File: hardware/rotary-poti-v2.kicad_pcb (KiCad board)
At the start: 2 copper layers, 30 x 25 mm, 22 parts, among them P1 CON-SENSOR2, P2 DEBUG, P3 BOOT, U1 XMC1XXX24, U3 DRILL, U4 DRILL, U5 DRILL, U6 DRILL

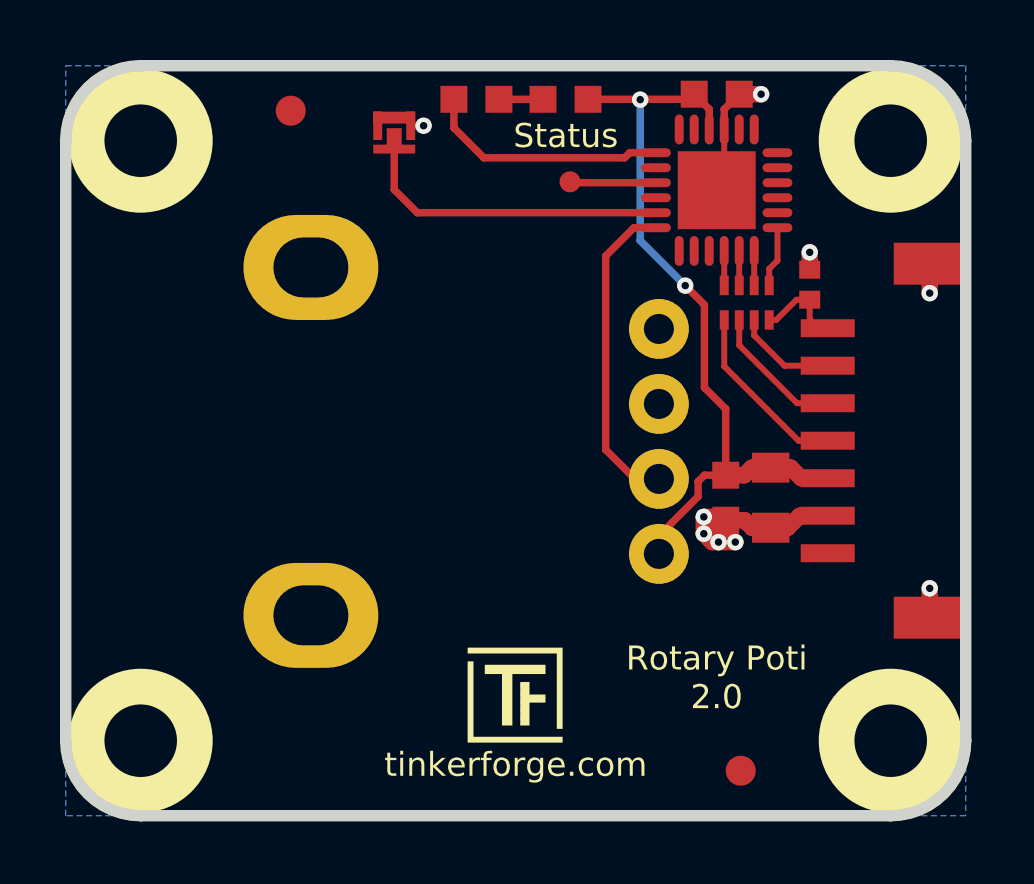
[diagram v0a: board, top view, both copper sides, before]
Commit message: Fix pin of IN_1
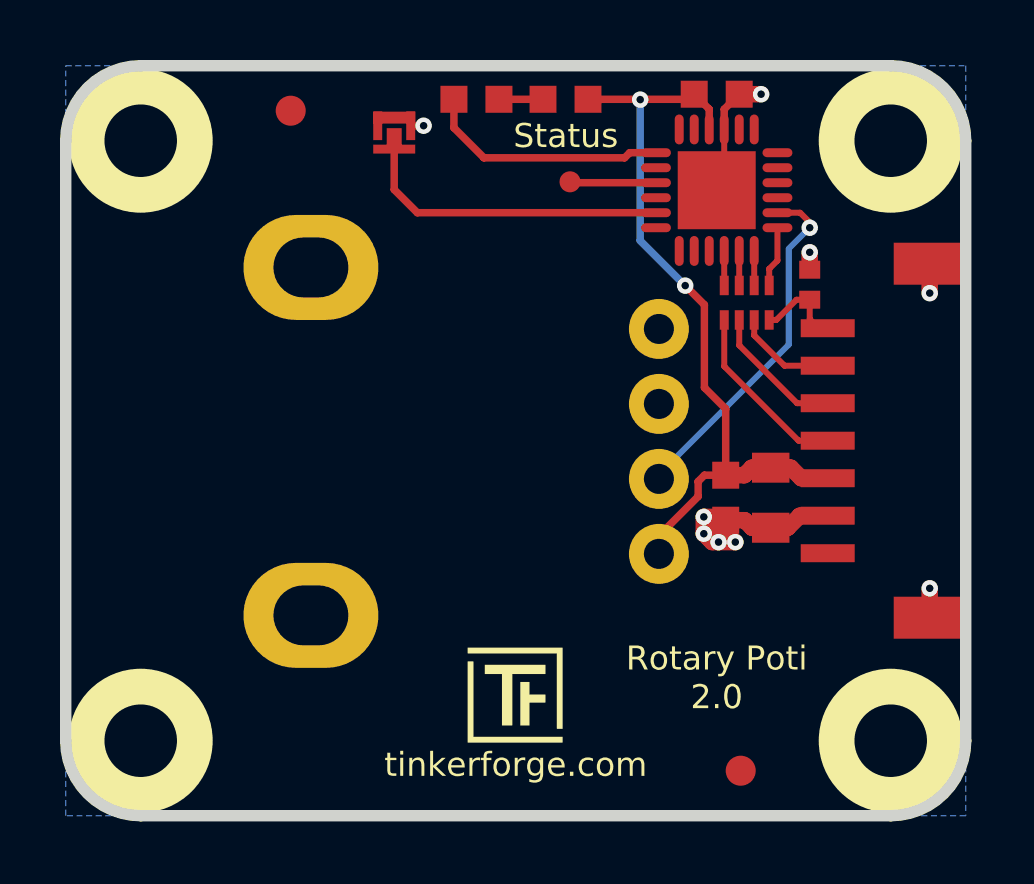
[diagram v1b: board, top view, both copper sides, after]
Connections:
- U1 pad 18: IN_1 -> Net-(U1-Pad18)
- U1 pad 2: Net-(U1-Pad2) -> IN_1
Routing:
- net IN_1: track 10.7 -> 11.8 mm, vias 0 -> 1
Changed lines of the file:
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@@
     (thickness 1.6002)
     (drawings 12)
-    (tracks 121)
+    (tracks 124)
     (zones 0)
     (modules 22)
@@
   )
   (setup
-    (last_trace_width 0.25)
+    (last_trace_width 0.2)
     (user_trace_width 0.2)
     (user_trace_width 0.25)
@@
   (net 15 S-CLK)
   (net 16 S-CS)
-  (net 17 "Net-(U1-Pad2)")
-  (net 18 "Net-(U1-Pad3)")
-  (net 19 "Net-(U1-Pad4)")
-  (net 20 "Net-(U1-Pad5)")
-  (net 21 "Net-(U1-Pad6)")
-  (net 22 "Net-(U1-Pad7)")
-  (net 23 "Net-(U1-Pad8)")
-  (net 24 "Net-(U1-Pad11)")
-  (net 25 "Net-(U1-Pad12)")
-  (net 26 "Net-(U1-Pad14)")
-  (net 27 "Net-(U1-Pad16)")
-  (net 28 "Net-(U1-Pad19)")
-  (net 29 "Net-(U1-Pad20)")
-  (net 30 "Net-(U1-Pad21)")
+  (net 17 "Net-(U1-Pad3)")
+  (net 18 "Net-(U1-Pad4)")
+  (net 19 "Net-(U1-Pad5)")
+  (net 20 "Net-(U1-Pad6)")
+  (net 21 "Net-(U1-Pad7)")
+  (net 22 "Net-(U1-Pad8)")
+  (net 23 "Net-(U1-Pad11)")
+  (net 24 "Net-(U1-Pad12)")
+  (net 25 "Net-(U1-Pad14)")
+  (net 26 "Net-(U1-Pad16)")
+  (net 27 "Net-(U1-Pad19)")
+  (net 28 "Net-(U1-Pad20)")
+  (net 29 "Net-(U1-Pad21)")
+  (net 30 "Net-(U1-Pad18)")
   (net_class Default "Dies ist die voreingestellte Netzklasse."
     (clearance 0.15)
@@
     (add_net "Net-(U1-Pad14)")
     (add_net "Net-(U1-Pad16)")
+    (add_net "Net-(U1-Pad18)")
     (add_net "Net-(U1-Pad19)")
-    (add_net "Net-(U1-Pad2)")
     (add_net "Net-(U1-Pad20)")
     (add_net "Net-(U1-Pad21)")
@@
       (net 13 S-MISO))
     (pad 2 smd oval (at -2.025 -0.75 180) (size 1 0.3) (layers Vorderseite F.Paste F.Mask)
-      (net 17 "Net-(U1-Pad2)"))
+      (net 2 IN_1))
     (pad 3 smd oval (at -2.025 -0.25 180) (size 1 0.3) (layers Vorderseite F.Paste F.Mask)
-      (net 18 "Net-(U1-Pad3)"))
+      (net 17 "Net-(U1-Pad3)"))
     (pad 4 smd oval (at -2.025 0.25 180) (size 1 0.3) (layers Vorderseite F.Paste F.Mask)
-      (net 19 "Net-(U1-Pad4)"))
+      (net 18 "Net-(U1-Pad4)"))
     (pad 5 smd oval (at -2.025 0.75 180) (size 1 0.3) (layers Vorderseite F.Paste F.Mask)
-      (net 20 "Net-(U1-Pad5)"))
+      (net 19 "Net-(U1-Pad5)"))
     (pad 6 smd oval (at -2.025 1.25 180) (size 1 0.3) (layers Vorderseite F.Paste F.Mask)
-      (net 21 "Net-(U1-Pad6)"))
+      (net 20 "Net-(U1-Pad6)"))
     (pad 7 smd oval (at -1.25 2.025 270) (size 1 0.3) (layers Vorderseite F.Paste F.Mask)
-      (net 22 "Net-(U1-Pad7)"))
+      (net 21 "Net-(U1-Pad7)"))
     (pad 8 smd oval (at -0.75 2.025 270) (size 1 0.3) (layers Vorderseite F.Paste F.Mask)
-      (net 23 "Net-(U1-Pad8)"))
+      (net 22 "Net-(U1-Pad8)"))
     (pad 9 smd oval (at -0.25 2.025 270) (size 1 0.3) (layers Vorderseite F.Paste F.Mask)
       (net 1 GND))
@@
       (net 3 VCC))
     (pad 11 smd oval (at 0.75 2.025 270) (size 1 0.3) (layers Vorderseite F.Paste F.Mask)
-      (net 24 "Net-(U1-Pad11)"))
+      (net 23 "Net-(U1-Pad11)"))
     (pad 12 smd oval (at 1.25 2.025 270) (size 1 0.3) (layers Vorderseite F.Paste F.Mask)
-      (net 25 "Net-(U1-Pad12)"))
+      (net 24 "Net-(U1-Pad12)"))
     (pad 13 smd oval (at 2.025 1.25 180) (size 1 0.3) (layers Vorderseite F.Paste F.Mask)
       (net 12 "Net-(R3-Pad1)"))
     (pad 14 smd oval (at 2.025 0.75 180) (size 1 0.3) (layers Vorderseite F.Paste F.Mask)
-      (net 26 "Net-(U1-Pad14)"))
+      (net 25 "Net-(U1-Pad14)"))
     (pad 15 smd oval (at 2.025 0.25 180) (size 1 0.3) (layers Vorderseite F.Paste F.Mask)
       (net 10 "Net-(P2-Pad1)"))
     (pad 16 smd oval (at 2.025 -0.25 180) (size 1 0.3) (layers Vorderseite F.Paste F.Mask)
-      (net 27 "Net-(U1-Pad16)"))
+      (net 26 "Net-(U1-Pad16)"))
     (pad 17 smd oval (at 2.025 -0.75 180) (size 1 0.3) (layers Vorderseite F.Paste F.Mask)
       (net 11 "Net-(P3-Pad2)"))
     (pad 18 smd oval (at 2.025 -1.25 180) (size 1 0.3) (layers Vorderseite F.Paste F.Mask)
-      (net 2 IN_1))
+      (net 30 "Net-(U1-Pad18)"))
     (pad 19 smd oval (at 1.25 -2.025 270) (size 1 0.3) (layers Vorderseite F.Paste F.Mask)
-      (net 28 "Net-(U1-Pad19)"))
+      (net 27 "Net-(U1-Pad19)"))
     (pad 20 smd oval (at 0.75 -2.025 270) (size 1 0.3) (layers Vorderseite F.Paste F.Mask)
-      (net 29 "Net-(U1-Pad20)"))
+      (net 28 "Net-(U1-Pad20)"))
     (pad 21 smd oval (at 0.25 -2.025 270) (size 1 0.3) (layers Vorderseite F.Paste F.Mask)
-      (net 30 "Net-(U1-Pad21)"))
+      (net 29 "Net-(U1-Pad21)"))
     (pad 22 smd oval (at -0.25 -2.025 270) (size 1 0.3) (layers Vorderseite F.Paste F.Mask)
       (net 16 S-CS))
@@
   (segment (start 153.0731 100.87356) (end 153.07564 100.87356) (width 0.29972) (layer Vorderseite) (net 1) (status 400))
   (segment (start 153.0731 100.87356) (end 153.07564 100.87356) (width 0.29972) (layer Rückseite) (net 1) (status 400))
-  (segment (start 153.0731 103.37292) (end 152.27292 103.37292) (width 0.25) (layer Vorderseite) (net 2))
-  (segment (start 152.27292 103.37292) (end 151.3 102.4) (width 0.25) (layer Vorderseite) (net 2))
-  (segment (start 151.3 102.4) (end 151.3 95.94) (width 0.25) (layer Vorderseite) (net 2))
-  (segment (start 151.3 95.94) (end 152.24 95) (width 0.25) (layer Vorderseite) (net 2))
-  (segment (start 152.24 95) (end 152.975 95) (width 0.25) (layer Vorderseite) (net 2))
+  (segment (start 158.1 95) (end 158.1 94.82) (width 0.2) (layer Vorderseite) (net 2))
+  (segment (start 157.78 94.5) (end 157.025 94.5) (width 0.2) (layer Vorderseite) (net 2))
+  (segment (start 158.1 94.82) (end 157.78 94.5) (width 0.2) (layer Vorderseite) (net 2))
+  (segment (start 153.0731 103.37292) (end 153.0731 103.2269) (width 0.2) (layer Rückseite) (net 2))
+  (segment (start 153.0731 103.2269) (end 157.4 98.9) (width 0.2) (layer Rückseite) (net 2))
+  (segment (start 157.4 98.9) (end 157.4 95.7) (width 0.2) (layer Rückseite) (net 2))
+  (segment (start 157.4 95.7) (end 158.1 95) (width 0.2) (layer Rückseite) (net 2))
+  (via (at 158.1 95) (size 0.55) (drill 0.24892) (layers Vorderseite Rückseite) (net 2))
   (segment (start 153.0731 105.87228) (end 153.0731 105.2669) (width 0.25) (layer Vorderseite) (net 3))
   (segment (start 153.0731 105.2669) (end 154.38 103.96) (width 0.25) (layer Vorderseite) (net 3))

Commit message: Fix origin
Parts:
- moved VAL 0.14 mm to (157.3, 102.2)
- moved VAL 0.14 mm to (149.3, 102.2)
- moved Ref** 0.14 mm to (146.8, 109.1)
- moved C5 0.14 mm to (155.1, 90.7)
- moved Fiducial_Mark 0.14 mm to (155.9, 113.2)
- moved Fiducial_Mark 0.14 mm to (140.9, 91.2)
- moved G*** 0.14 mm to (141.9, 102.2)
- moved P1 0.14 mm to (163.4, 102.2)
- moved P3 0.14 mm to (144.3, 91.9)
- moved RV1 0.14 mm to (147.7, 102.2)
- moved U3 0.14 mm to (135.9, 112.2)
- moved U4 0.14 mm to (160.9, 92.2)
- moved U5 0.14 mm to (160.9, 112.2)
- moved U6 0.14 mm to (135.9, 92.2)
- moved C1 0.14 mm to (158.2, 97.0)
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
